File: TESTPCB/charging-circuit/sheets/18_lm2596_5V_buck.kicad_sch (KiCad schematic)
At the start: 15 parts, among them J20 Conn_01x01_Pin, J21 Conn_01x01_Pin, J22 Conn_01x01_Pin, J23 Conn_01x01_Pin, U30 LM2596S-ADJ

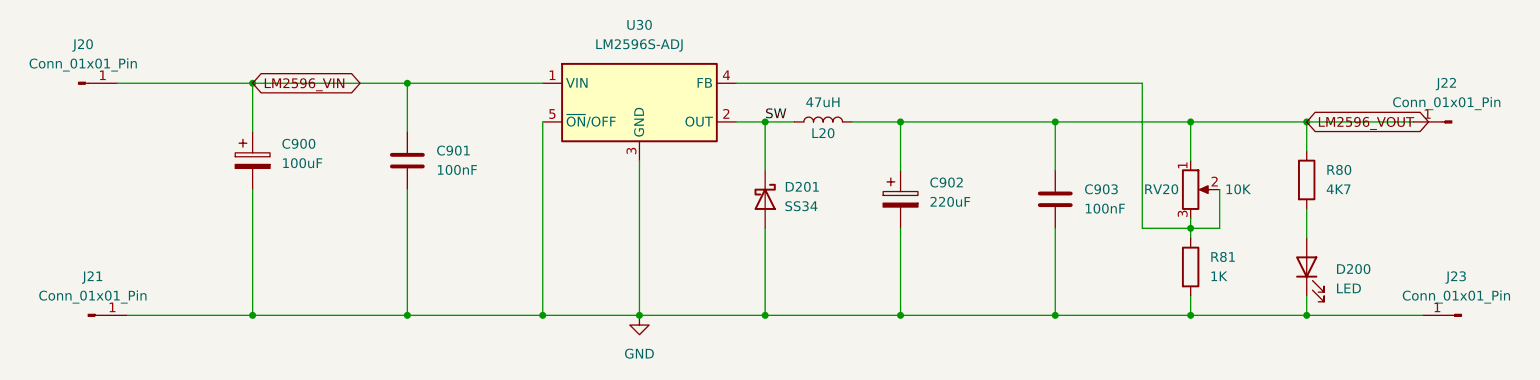
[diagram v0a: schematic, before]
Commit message: added 5V buck
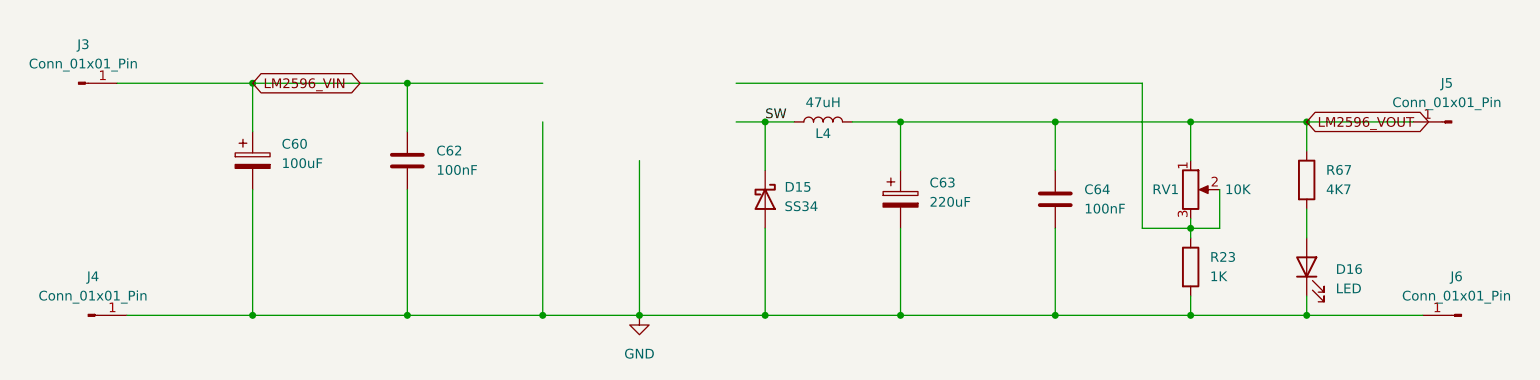
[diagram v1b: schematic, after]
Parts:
- removed U30: LM2596S-ADJ, Package_TO_SOT_SMD:TO-263-5_TabPin3, symbol Regulator_Switching:LM2596S-ADJ
- renumbered C900 to C60, C901 to C62, C902 to C63, C903 to C64, D201 to D15, D200 to D16, J20 to J3, J21 to J4, J22 to J5, J23 to J6, L20 to L4, R81 to R23, R80 to R67, RV20 to RV1
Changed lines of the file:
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@@
 		(on_board yes)
 		(dnp no)
-		(property "Reference" "L20"
+		(property "Reference" "L4"
 			(at 156.21 95.504 90)
 			(effects
@@
 		(dnp no)
 		(fields_autoplaced yes)
-		(property "Reference" "D201"
+		(property "Reference" "D15"
 			(at 151.13 102.5524 90)
 			(effects
@@
 		(dnp no)
 		(fields_autoplaced yes)
-		(property "Reference" "C901"
+		(property "Reference" "C62"
 			(at 105.41 97.7899 0)
 			(effects
@@
 		(dnp no)
 		(fields_autoplaced yes)
-		(property "Reference" "J23"
+		(property "Reference" "J6"
 			(at 239.395 114.3 0)
 			(effects
@@
 		(dnp no)
 		(fields_autoplaced yes)
-		(property "Reference" "#PWR01"
+		(property "Reference" "#PWR02"
 			(at 132.08 125.73 0)
 			(effects
@@
 		(dnp no)
 		(fields_autoplaced yes)
-		(property "Reference" "C902"
+		(property "Reference" "C63"
 			(at 170.18 101.9809 0)
 			(effects
@@
 		(dnp no)
 		(fields_autoplaced yes)
-		(property "Reference" "J20"
+		(property "Reference" "J3"
 			(at 59.055 83.82 0)
 			(effects
@@
 		(on_board yes)
 		(dnp no)
-		(property "Reference" "RV20"
+		(property "Reference" "RV1"
 			(at 202.946 102.87 0)
 			(effects
@@
 		(dnp no)
 		(fields_autoplaced yes)
-		(property "Reference" "D200"
+		(property "Reference" "D16"
 			(at 223.52 113.3474 90)
 			(effects
@@
 		(dnp no)
 		(fields_autoplaced yes)
-		(property "Reference" "R80"
+		(property "Reference" "R67"
 			(at 222.25 100.3299 0)
 			(effects
@@
 		(dnp no)
 		(fields_autoplaced yes)
-		(property "Reference" "R81"
+		(property "Reference" "R23"
 			(at 207.01 111.7599 0)
 			(effects
@@
 	)
 	(symbol
-		(lib_id "Regulator_Switching:LM2596S-ADJ")
-		(at 132.08 91.44 0)
-		(unit 1)
-		(exclude_from_sim no)
-		(in_bom yes)
-		(on_board yes)
-		(dnp no)
-		(fields_autoplaced yes)
-		(property "Reference" "U30"
-			(at 132.08 81.28 0)
-			(effects
-				(font
-					(size 1.27 1.27)
-				)
-			)
-		)
-		(property "Value" "LM2596S-ADJ"
-			(at 132.08 83.82 0)
-			(effects
-				(font
-					(size 1.27 1.27)
-				)
-			)
-		)
-		(property "Footprint" "Package_TO_SOT_SMD:TO-263-5_TabPin3"
-			(at 133.35 97.79 0)
-			(effects
-				(font
-					(size 1.27 1.27)
-					(italic yes)
-				)
-				(justify left)
-				(hide yes)
-			)
-		)
-		(property "Datasheet" "http://www.ti.com/lit/ds/symlink/lm2596.pdf"
-			(at 132.08 91.44 0)
-			(effects
-				(font
-					(size 1.27 1.27)
-				)
-				(hide yes)
-			)
-		)
-		(property "Description" "Adjustable 3A Step-Down Voltage Regulator, TO-263"
-			(at 132.08 91.44 0)
-			(effects
-				(font
-					(size 1.27 1.27)
-				)
-				(hide yes)
-			)
-		)
-		(pin "1"
-		)
-		(pin "4"
-		)
-		(pin "3"
-		)
-		(pin "2"
-		)
-		(pin "5"
-		)
-		(instances
-			(project "charging-circuit"
-				(path "/529bc8a5-ffae-43ac-972d-caccc3afab85/9dddee0f-db6b-4d06-95d5-93553e494b2c"
-					(reference "U30")
-					(unit 1)
-				)
-				(path "/529bc8a5-ffae-43ac-972d-caccc3afab85/e6612f6f-e131-40dc-9b50-f62250179b84"
-					(reference "U18")
-					(unit 1)
-				)
-			)
-		)
-	)
-	(symbol
 		(lib_id "Connector:Conn_01x01_Pin")
 		(at 238.76 93.98 180)
@@
 		(dnp no)
 		(fields_autoplaced yes)
-		(property "Reference" "J22"
+		(property "Reference" "J5"
 			(at 238.125 88.9 0)
 			(effects
@@
 		(dnp no)
 		(fields_autoplaced yes)
-		(property "Reference" "C903"
+		(property "Reference" "C64"
 			(at 190.5 102.8699 0)
 			(effects
@@
 		(dnp no)
 		(fields_autoplaced yes)
-		(property "Reference" "C900"
+		(property "Reference" "C60"
 			(at 85.09 96.9009 0)
 			(effects
@@
 		(dnp no)
 		(fields_autoplaced yes)
-		(property "Reference" "J21"
+		(property "Reference" "J4"
 			(at 60.325 114.3 0)
 			(effects
@@
 		)
 	)
-	(sheet_instances
-		(path "/"
-			(page "1")
-		)
-	)
-	(embedded_fonts no)
 )

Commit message: Fixed issue with footprint not showing up and took off potentiometer
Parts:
- removed R23: 1K, Resistor_SMD:R_0603_1608Metric, symbol Device:R
- removed RV1: 10K, Potentiometer_THT:Potentiometer_Bourns_3296W_Vertical, symbol Device:R_Potentiometer
- added U18: LM2596SX-5.0/NOPB, easyeda2kicad:TO-263-5_L10.2-W8.9-P1.70-TL, symbol easyeda2kicad:LM2596SX-5.0_NOPB
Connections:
- net GND: now also U18.3 (GND), U18.5 (~{ON}/OFF)
- net LM2596_VIN: now also U18.1 (VIN)
- net LM2596_VOUT: now also U18.4 (FB)
- net SW: now also U18.2 (OUT)
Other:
- moved on the sheet: D16, J5, J6, R67

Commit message: changed to 5v
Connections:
- net LM2596_VIN renamed LM2596_5V_VIN
- net LM2596_VOUT renamed LM2596_5V_VOUT
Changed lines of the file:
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@@
 		)
 	)
-	(global_label "LM2596_VOUT"
+	(global_label "LM2596_5V_VOUT"
 		(shape bidirectional)
 		(at 207.01 93.98 0)
@@
 		)
 	)
-	(global_label "LM2596_VIN"
+	(global_label "LM2596_5V_VIN"
 		(shape bidirectional)
 		(at 81.28 88.9 0)

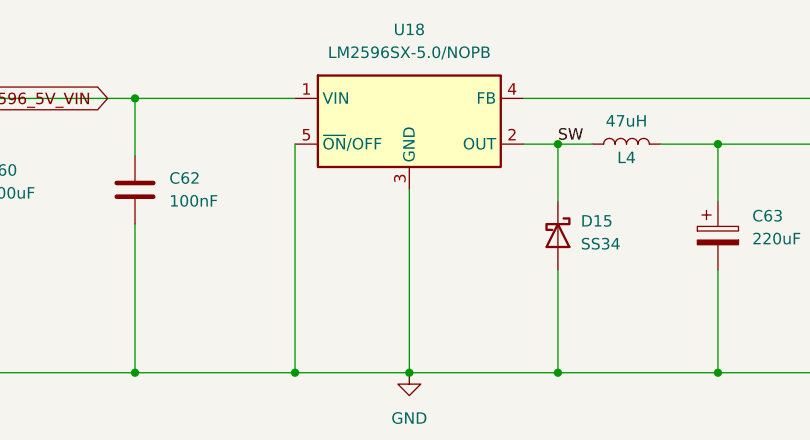
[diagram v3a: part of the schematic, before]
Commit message: added pin 6 to gnd
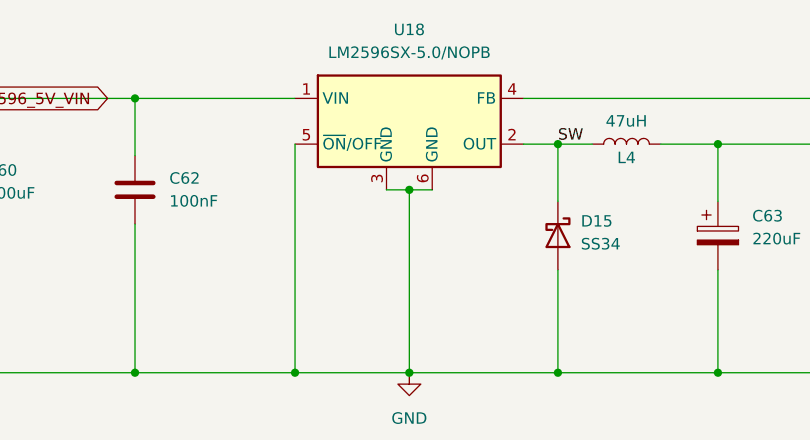
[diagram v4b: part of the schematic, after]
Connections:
- net GND: now also U18.6 (GND)
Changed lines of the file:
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@@
+	)
+	(junction
+		(at 132.08 99.06)
+		(diameter 0)
+		(color 0 0 0 0)
 	)
 	(junction
@@
 	(wire
 		(pts
+			(xy 129.54 99.06) (xy 132.08 99.06)
+		)
+		(stroke
+			(width 0)
+			(type default)
+		)
+	)
+	(wire
+		(pts
 			(xy 186.69 93.98) (xy 207.01 93.98)
 		)
@@
 		(pts
 			(xy 186.69 119.38) (xy 207.01 119.38)
+		)
+		(stroke
+			(width 0)
+			(type default)
+		)
+	)
+	(wire
+		(pts
+			(xy 132.08 99.06) (xy 134.62 99.06)
 		)
 		(stroke
@@
 		(pin "1"
 		)
+		(pin "6"
+		)
 		(instances
